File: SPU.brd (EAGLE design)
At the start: 160 x 130 mm, 421 parts, among them Q1 BSS123, Q2 12MHz, Q3 BSS123, Q4 BSS123, Q5 BSS123, Q6 BSS123, Y1 32.768kHz

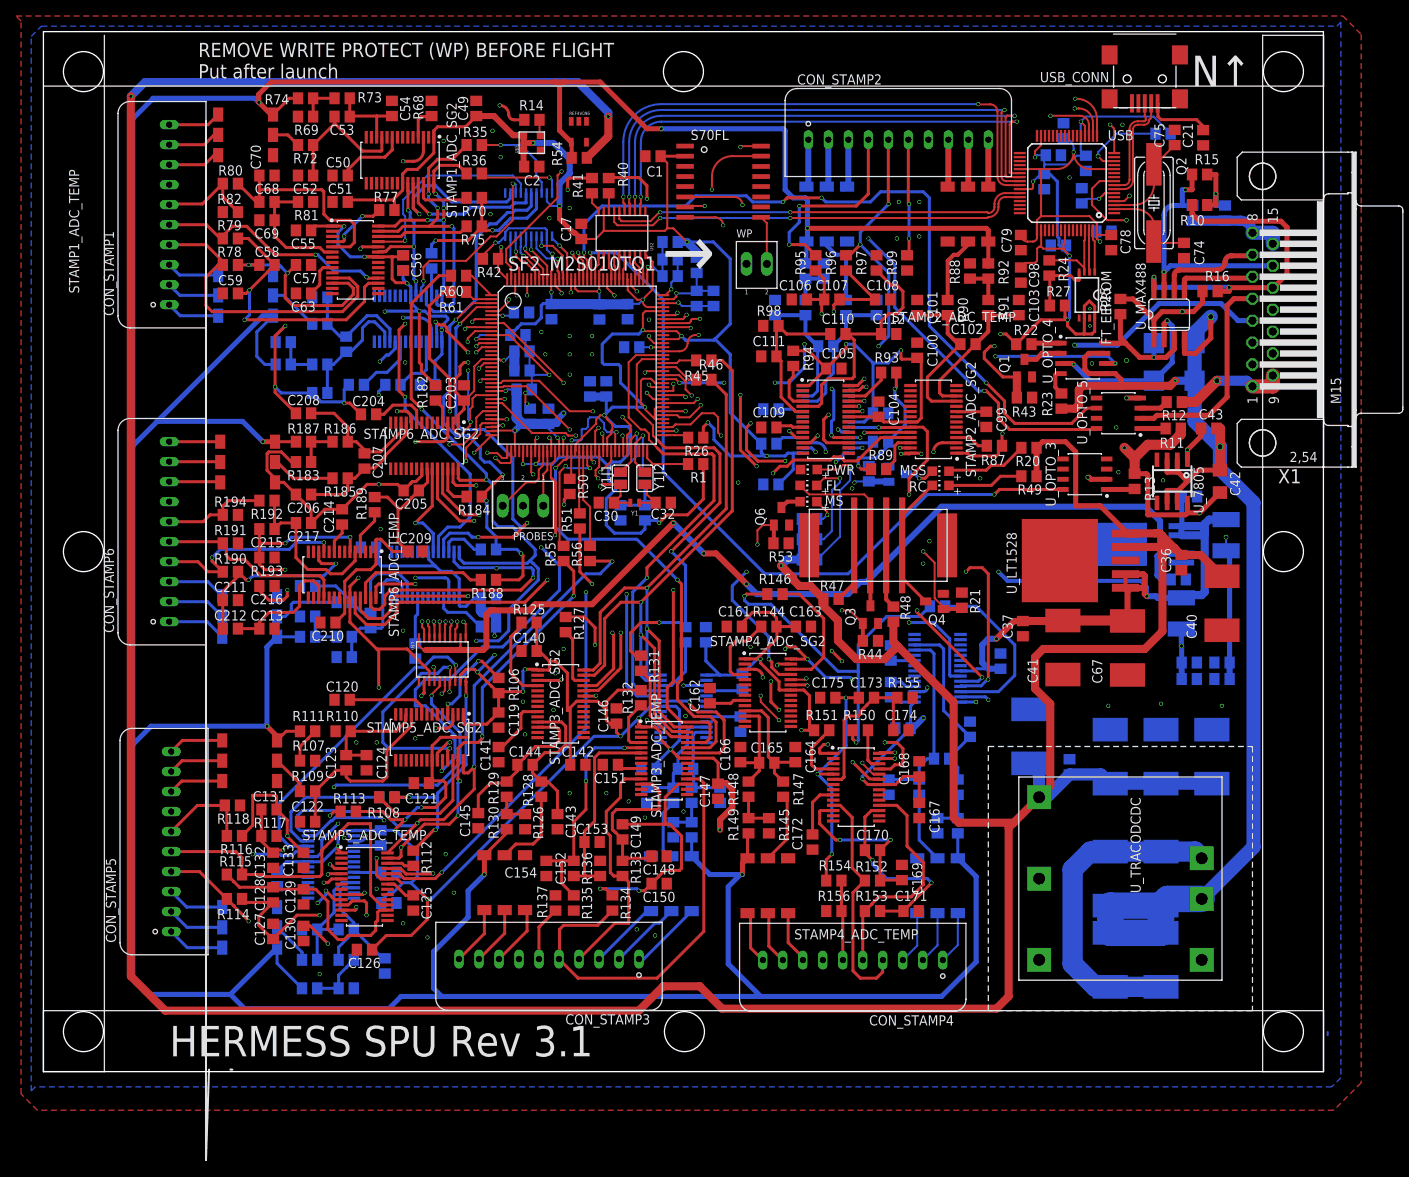
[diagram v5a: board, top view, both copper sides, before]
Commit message: Routing completed DRC: Run successfully Adding via fences Resolved grounding problems NOTE: USB Port position changed NOTE: Run ratsnest before generating gerber files
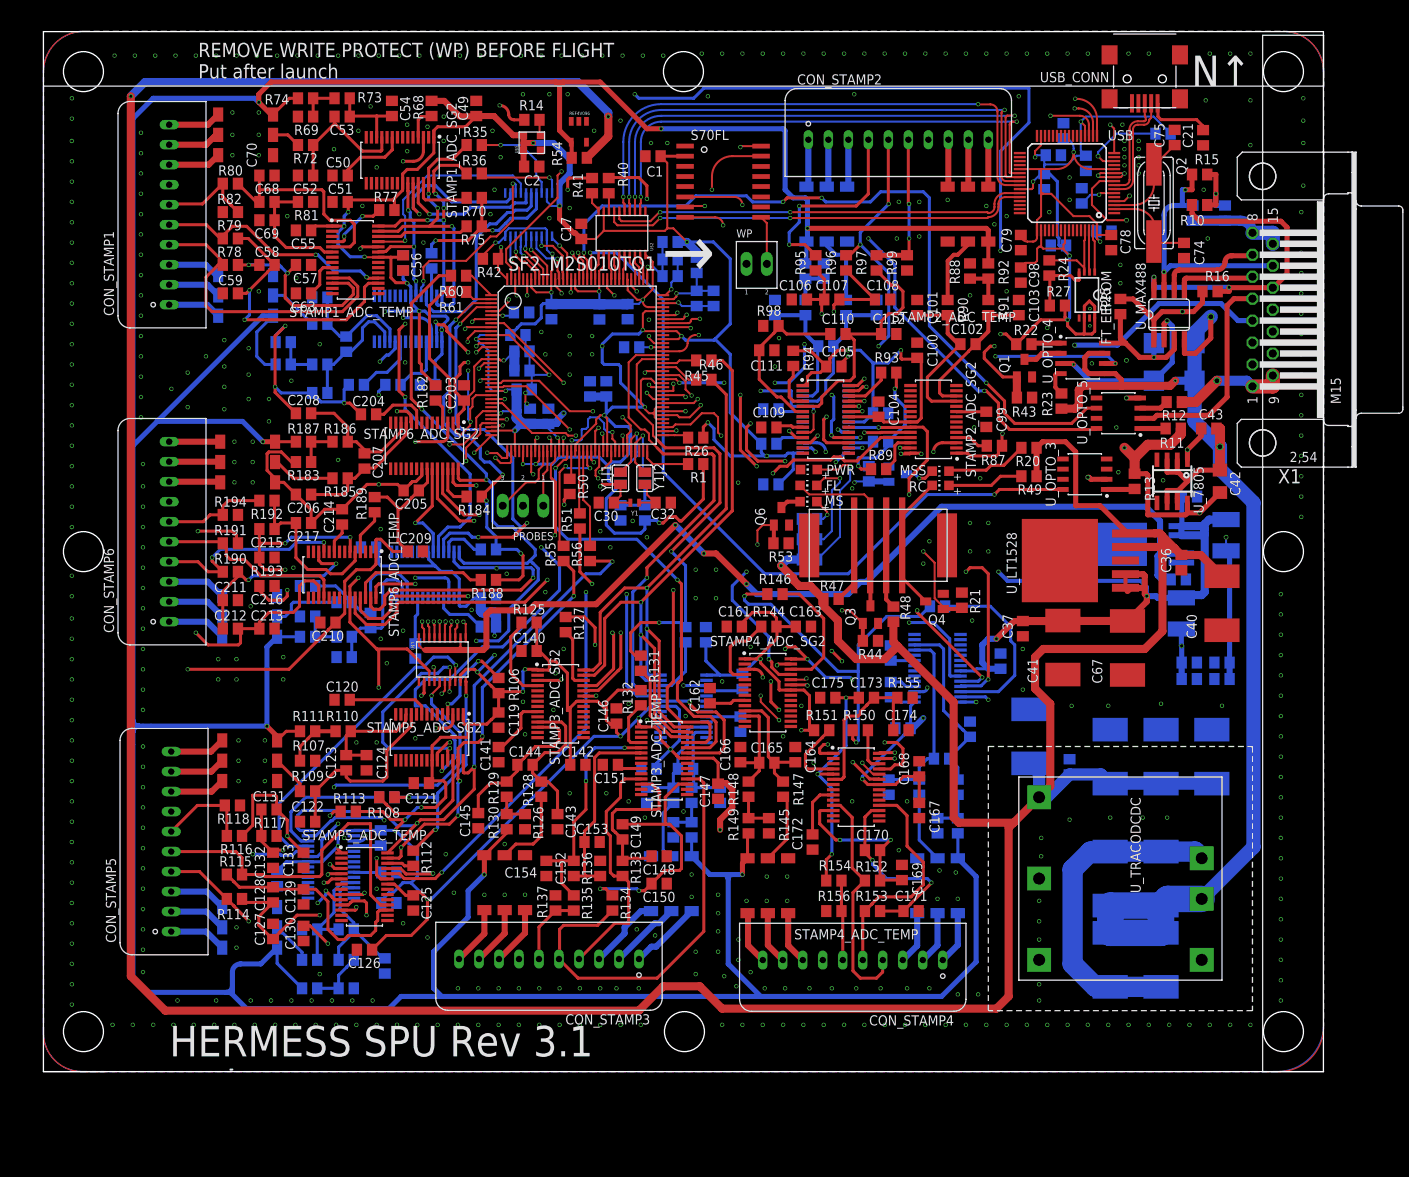
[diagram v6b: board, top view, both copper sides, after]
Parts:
- moved C111 0.80 mm to (90.4, 90.2), turned to 0 degrees
- moved C105 0.25 mm to (98.8, 88.1)
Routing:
- net 3V3: track 1106.0 -> 1401.2 mm, vias 53 -> 58
- net N$213: track 16.3 -> 43.9 mm, vias 0 -> 2
- net 1V2: track 248.6 -> 273.0 mm, vias 14 -> 15
- net GND: track 210.5 -> 232.0 mm, vias 90 -> 513
- net STAMP2_TEMP_AIN3: track 14.6 -> 18.4 mm
- net 4V096: track 546.2 -> 549.9 mm
- net N$124: track 4.47 -> 7.02 mm
- net S2AT2: track 19.6 -> 21.9 mm
- net STAMP3_TEMP_AIN3: track 6.92 -> 9.20 mm
- net STAMP1_SG2_AIN2: track 6.63 -> 8.62 mm
- net N$179: track 40.2 -> 42.1 mm
- net ADC_START: track 301.6 -> 299.7 mm
- net 5V: track 508.0 -> 509.4 mm
- net N$169: track 8.17 -> 9.40 mm
- net N$156: track 22.1 -> 23.2 mm
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
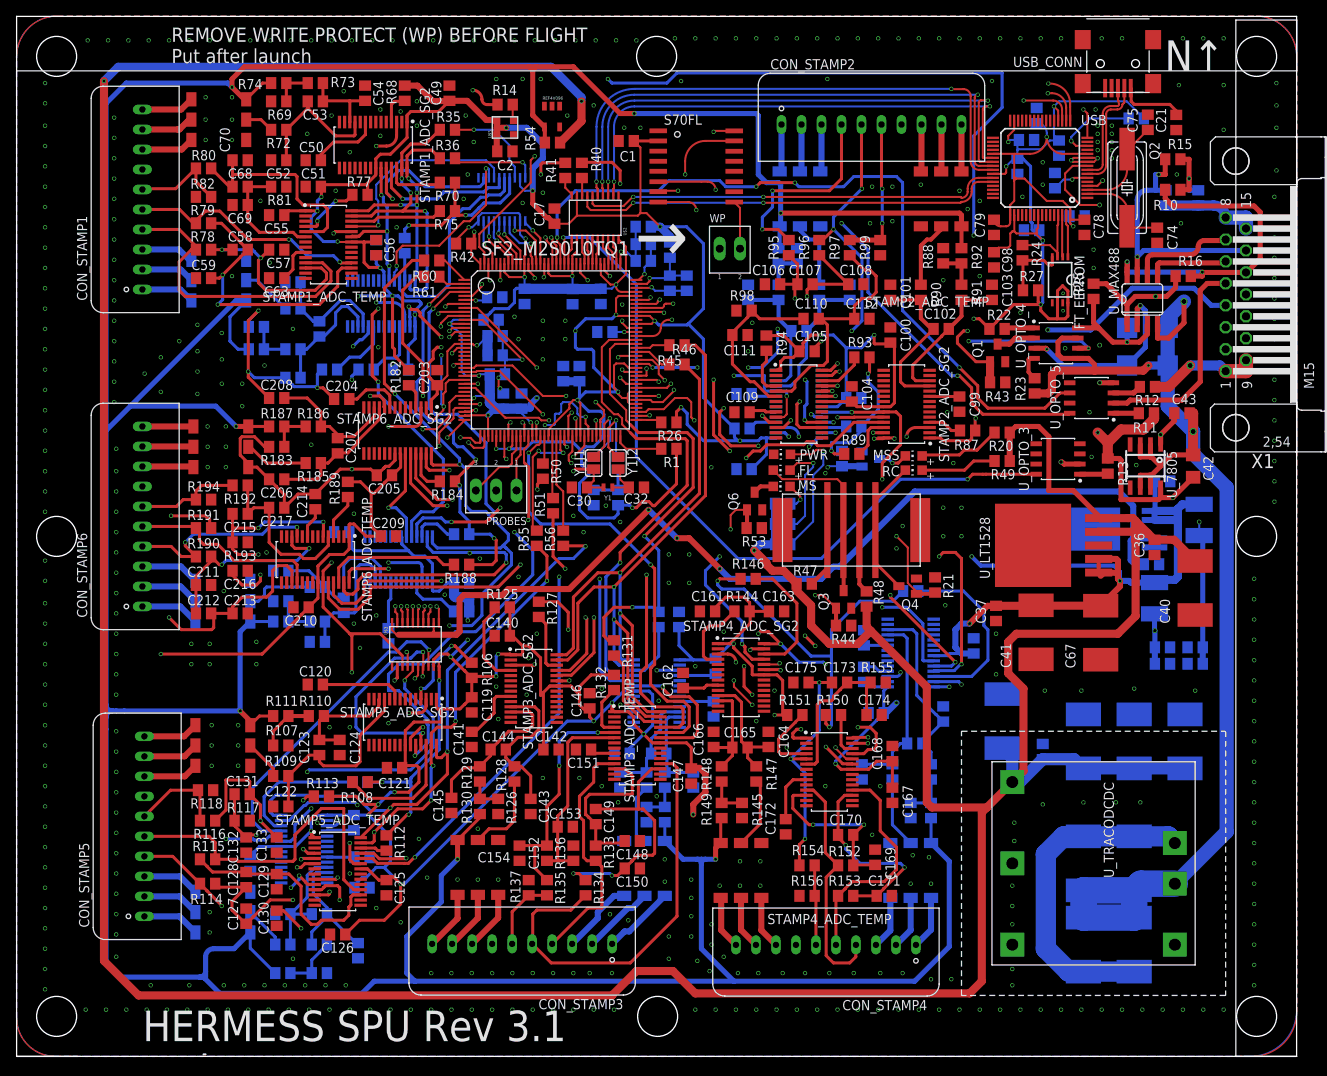
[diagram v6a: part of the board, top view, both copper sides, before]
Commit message: Routing completed DRC: Run successfully Adding via fences Resolved grounding problems NOTE: USB Port position changed NOTE: Run ratsnest before generating gerber files
NOTE: Second commit, same topic due to previous staged changes.
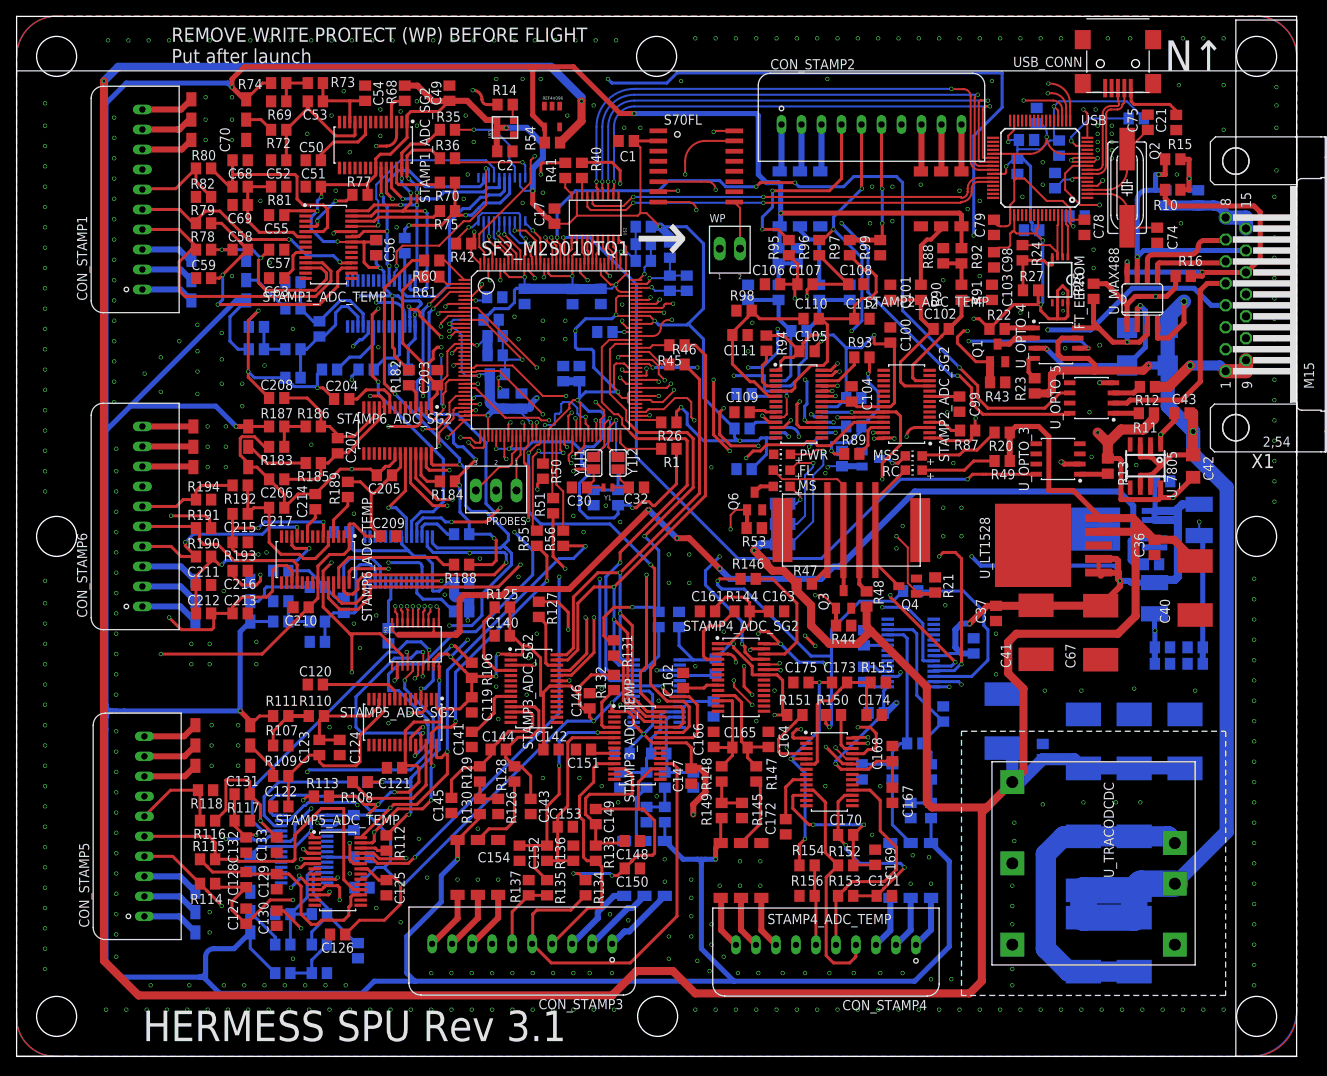
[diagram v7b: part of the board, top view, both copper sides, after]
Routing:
- net GND: vias 513 -> 505
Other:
- board text added: "J. Lusky, R. Grimsmann"
- board text added: "Nov. 2021"
- board text added: "Short 5V - GND to activate FLOMESS MODE"
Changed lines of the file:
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@@
 <drawing>
 <settings>
-<setting alwaysvectorfont="no"/>
+<setting alwaysvectorfont="yes"/>
 <setting verticaltext="up"/>
 </settings>
@@
 <wire x1="160.02" y1="129.54" x2="160.02" y2="123.19" width="0.1524" layer="21"/>
 <wire x1="160.02" y1="123.19" x2="0" y2="123.19" width="0.1524" layer="21"/>
-<wire x1="23.368" y1="0.254" x2="23.622" y2="0.254" width="0.254" layer="21"/>
 <dimension x1="143.002" y1="127.762" x2="132.207" y2="127.7366" x3="137.58531875" y3="135.899965625" textsize="1.778" layer="47"/>
+<text x="150.622" y="3.302" size="1.778" layer="22" rot="MR0">J. Lusky, R. Grimsmann</text>
+<text x="21.59" y="3.302" size="1.778" layer="22" rot="MR0">Nov. 2021</text>
+<text x="6.858" y="119.126" size="1.778" layer="22" rot="MR270">Short 5V - GND to activate FLOMESS MODE</text>
 </plain>
 <attributes>
@@
 <via x="39.878" y="108.204" extent="1-16" drill="0.35"/>
 <via x="3.556" y="59.436" extent="1-16" drill="0.35"/>
-<via x="3.556" y="61.976" extent="1-16" drill="0.35"/>
 <via x="12.446" y="12.446" extent="1-16" drill="0.35"/>
 <via x="12.446" y="15.24" extent="1-16" drill="0.35"/>
@@
 <via x="12.446" y="70.612" extent="1-16" drill="0.35"/>
 <via x="12.446" y="73.152" extent="1-16" drill="0.35"/>
-<via x="3.556" y="8.382" extent="1-16" drill="0.35"/>
 <via x="3.556" y="10.922" extent="1-16" drill="0.35"/>
 <via x="3.556" y="13.462" extent="1-16" drill="0.35"/>
@@
 <via x="29.972" y="51.816" extent="1-16" drill="0.35"/>
 <via x="3.556" y="119.126" extent="1-16" drill="0.35"/>
-<via x="3.556" y="121.666" extent="1-16" drill="0.35"/>
-<via x="3.556" y="68.072" extent="1-16" drill="0.35"/>
 <via x="3.556" y="70.612" extent="1-16" drill="0.35"/>
 <via x="3.556" y="73.152" extent="1-16" drill="0.35"/>
@@
 <via x="12.192" y="114.808" extent="1-16" drill="0.35"/>
 <via x="12.192" y="117.348" extent="1-16" drill="0.35"/>
-<via x="8.89" y="127" extent="1-16" drill="0.35"/>
 <via x="11.43" y="127" extent="1-16" drill="0.35"/>
 <via x="13.97" y="127" extent="1-16" drill="0.35"/>
@@
 <via x="72.39" y="127" extent="1-16" drill="0.35"/>
 <via x="74.93" y="127" extent="1-16" drill="0.35"/>
-<via x="77.47" y="127" extent="1-16" drill="0.35"/>
-<via x="82.296" y="127.254" extent="1-16" drill="0.35"/>
 <via x="84.836" y="127.254" extent="1-16" drill="0.35"/>
 <via x="87.376" y="127.254" extent="1-16" drill="0.35"/>
@@
 <via x="128.016" y="127.254" extent="1-16" drill="0.35"/>
 <via x="130.556" y="127.254" extent="1-16" drill="0.35"/>
-<via x="135.636" y="127.254" extent="1-16" drill="0.35"/>
-<via x="138.176" y="127.254" extent="1-16" drill="0.35"/>
+<via x="136.398" y="127.254" extent="1-16" drill="0.35"/>
+<via x="139.192" y="127.254" extent="1-16" drill="0.35"/>
 <via x="22.606" y="82.804" extent="1-16" drill="0.35"/>
 <via x="25.654" y="84.074" extent="1-16" drill="0.35"/>
@@
 <via x="84.074" y="62.738" extent="1-16" drill="0.35"/>
 <via x="75.438" y="66.802" extent="1-16" drill="0.35"/>
-<via x="8.636" y="5.842" extent="1-16" drill="0.35"/>
 <via x="11.176" y="5.842" extent="1-16" drill="0.35"/>
 <via x="13.716" y="5.842" extent="1-16" drill="0.35"/>
@@
 <via x="157.226" y="82.042" extent="1-16" drill="0.35"/>
 <via x="157.226" y="84.582" extent="1-16" drill="0.35"/>
-<via x="157.48" y="121.666" extent="1-16" drill="0.35"/>
 <via x="157.48" y="116.078" extent="1-16" drill="0.35"/>
 <via x="157.226" y="87.122" extent="1-16" drill="0.35"/>
@@
 <via x="60.198" y="22.098" extent="1-16" drill="0.35"/>
 <via x="36.83" y="76.454" extent="1-16" drill="0.35"/>
+<via x="157.48" y="121.158" extent="1-16" drill="0.35"/>
 </signal>
 <signal name="3V3">
